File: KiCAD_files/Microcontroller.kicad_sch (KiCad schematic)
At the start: 87 parts, among them J403 RJ45_LED_Shielded, J404 RJ45_LED_Shielded, J405 Conn_01x02_Male, J406 Conn_01x02_Male, P401 Power2, U401 OwnTech_SPIN, U402 TCAN334GDR, U403 MCP1799T-5002H/TT, U404 AP1117-50, U405 LTC2850xS8, U406 OPA2277, U407 OPA316

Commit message: Closed open issues on TWIST V1.2. Cleaned the schematic and tweaked the routing files
Signed-off-by: Jean Alinei <jean.alinei@laas.fr>
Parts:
- removed C403, C406, C407: 10uF, Footprints:C_1210_3225Metric, symbol Device:C_Small
- removed C404, C405, C408, C409: 1uF, Footprints:C_0805_2012Metric, symbol Device:C_Small
- removed D401, D402: RBR2MM60ATFTR, Diode_SMD:D_SOD-123, symbol Device:D_Schottky_Small
- removed JP402: SolderJumper_2_Open, Jumper:SolderJumper-2_P1.3mm_Open_Pad1.0x1.5mm, symbol Jumper:SolderJumper_2_Open
- removed PS401: TEA 1-0505, Footprints:Converter_DCDC_Murata_MEE1SxxxxSC_THT, symbol Converter_DCDC:MEE1S0505SC
- removed PS402: TBA 1-0512, Footprints:Converter_DCDC_Murata_MEE1SxxxxSC_THT, symbol Converter_DCDC:MEE1S0512SC
- removed R421: 4.7k, Footprints:R_0805_2012Metric, symbol Device:R
- removed R424: 1k, Footprints:R_0805_2012Metric, symbol Device:R_Small
- removed U403: MCP1799T-5002H/TT, Footprints:SOT-23_copy, symbol Regulator_Linear:MCP1754S-5002xCB
- removed U404: AP1117-50, Package_TO_SOT_SMD:SOT-223-3_TabPin2, symbol Regulator_Linear:AP1117-50
- added unit 4 of U401
- C402: value 10uF -> 15nF; footprint Footprints:C_1210_3225Metric -> Footprints:C_0805_2012Metric; #manf 12105C106KAT2A -> (none); Manf# 12105C106KAT2A -> CC0805JRNPO9BN200
- F401, F402: footprint Fuse:Fuse_0805_2012Metric -> Fuse:Fuse_1210_3225Metric
- R408: value 1R -> 120R; Manf# CR0805-J/-1R0ELF -> CR0805-FX-4701ELF
- U406: value OPA2277 -> MCP6487T-E/SN
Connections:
- net GND_COM is gone; now on net DGND: J403.8, J404.8, J405.2 (Pin_2), J406.2 (Pin_2), R403.1, R405.1
- net +3V3: now also U401.36 (+3.3V); no longer U401.42 (+3.3V)
- net +5VD: now also C413.1, C415.1, U401.40 (+VIN), U406.8 (V+), U407.5 (V+); no longer C402.1, U401.46 (+VIN)
- net +6V: now also F401.1, F402.2
- net +BATT: now also U401.39 (+VBAT); no longer U401.45 (+VBAT)
- net ADC2_IN5: now also U401.35 (PC4); no longer U401.41 (PC4)
- net ADC3_IN12: now also U401.31 (PB0); no longer U401.37 (PB0)
- net DAC2: now also U401.34 (PA6); no longer U401.40 (PA6)
- net DGND: now also C402.1, U401.23 (GND), U401.28 (GND), U401.33 (GND), U401.38 (GND), U401.54 (GND), U401.57 (GND); no longer C402.2, R408.2, U401.22 (GND), U401.25 (GND), U401.29 (GND), U401.34 (GND), U401.39 (GND), U401.44 (GND)
- net FDCAN1_{RX}: now also U401.58 (PB8); no longer U401.26 (PB8)
- net FDCAN1_{TX}: now also U401.21 (PB9); no longer U401.27 (PB9)
- net HRTIM_CHA1: now also U401.12 (PA8); no longer U401.14 (PA9)
- net HRTIM_CHA2: now also U401.14 (PA9); no longer U401.12 (PA8)
- net I_{I1Low}: now also U401.30 (PA1); no longer U401.36 (PA1)
- net I_{I2Low}: now also U401.25 (PC1); no longer U401.31 (PC1)
- net I_{IHigh}: now also U401.26 (PC2); no longer U401.32 (PC2)
- net PB1: now also U401.37 (PB1); no longer U401.43 (PB1)
- net PB6: now also U401.55 (PB6); no longer U401.23 (PB6)
- net PC13: now also U401.22 (PC13); no longer U401.28 (PC13)
- net SHARE+: no longer R420.2
- net V_{I1Low}: now also U401.29 (PA0); no longer U401.35 (PA0)
- net V_{I2Low}: now also U401.24 (PC0); no longer U401.30 (PC0)
- net V_{IHigh}: now also U401.27 (PC3); no longer U401.33 (PC3)
- net at R408.1: now also C411.1, R415.1, U406.7
- net at R419.1, U406.5 (+): now also R420.2
- net CAN1_STB: no longer names the net of U402.8 (STB)
- new net: C402.2, JP410.2 (B), JP411.2 (B), R408.2
- no-connect marks 21 -> 23
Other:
- note added: "1.024V reference for measurement offset"
- note added: "CAN bus power supply - 6V - 100mA Polyfuse to prevent over-current in daisy-chained bus with multiple sources and sinks."
- note added: "Emitting circuit"
- note added: "Low pass filter Cut-off frequency 88.5kHz"
- note added: "Receiving circuit"
- note removed: "Alternate 1.024V VREF signal from SoC integrated DAC2. Conflicts with Analog share bus"
- note removed: "CAN bus power supply - 6V - 100mA Diodes necessary to prevent separate GND loops. Polyfuse to prevent over-current in daisy-chained bus with multiple sources and sinks."
- note removed: "DAC2 can be used to provide a reference if this fails"
- note removed: "Rudimentary 1.024V reference for measurement offset"
- moved on the sheet: C401, C410, C411, C412, C413, C414, C415, C416, D403, F401, F402, J403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

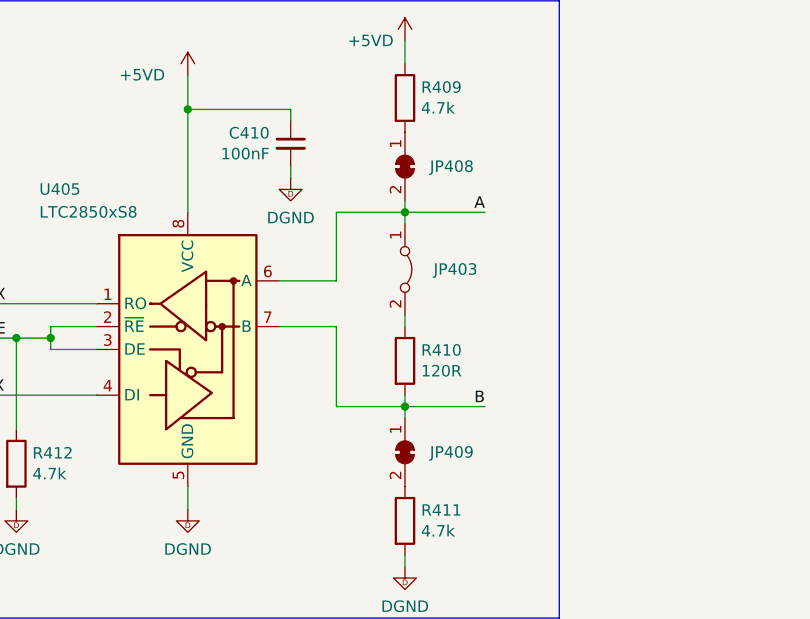
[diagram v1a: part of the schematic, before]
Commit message: Double check of each issue. Issue are now closed for V1.3
Signed-off-by: Jean Alinei <jean.alinei@laas.fr>
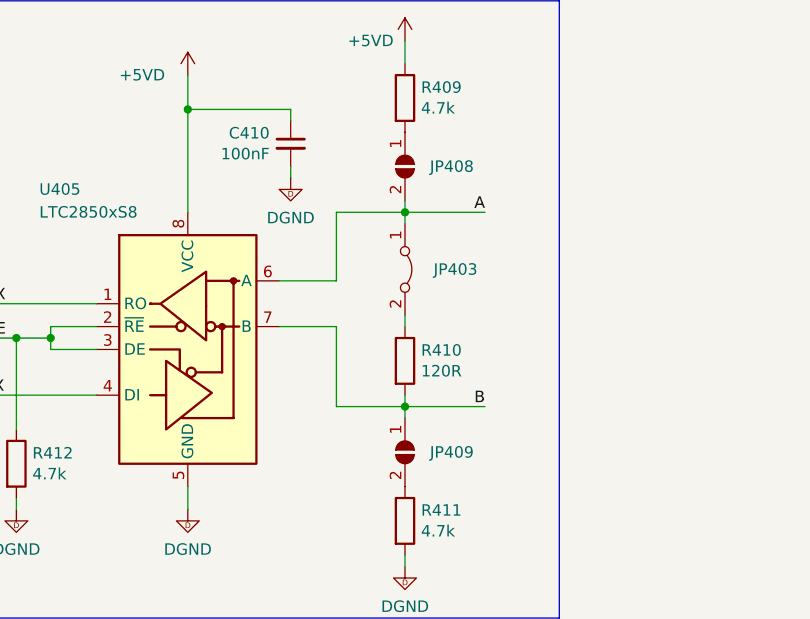
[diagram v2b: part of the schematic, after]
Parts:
- JP408, JP409: footprint Jumper:SolderJumper-2_P1.3mm_Bridged_Pad1.0x1.5mm -> Jumper:SolderJumper-2_P1.3mm_Open_RoundedPad1.0x1.5mm; symbol Jumper:SolderJumper_2_Bridged -> Jumper:SolderJumper_2_Open
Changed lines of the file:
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@@
     )
   )
-  (symbol (lib_id "Jumper:SolderJumper_2_Bridged") (at 264.16 171.45 270) (unit 1)
+  (symbol (lib_id "Jumper:SolderJumper_2_Open") (at 264.16 171.45 270) (unit 1)
     (in_bom yes) (on_board yes) (dnp no)
     (property "Reference" "JP409" (at 269.367 171.45 90)
@@
       (effects (font (size 1.27 1.27)) hide)
     )
-    (property "Footprint" "Jumper:SolderJumper-2_P1.3mm_Bridged_Pad1.0x1.5mm" (at 264.16 171.45 0)
+    (property "Footprint" "Jumper:SolderJumper-2_P1.3mm_Open_RoundedPad1.0x1.5mm" (at 264.16 171.45 0)
       (effects (font (size 1.27 1.27)) hide)
     )
@@
     )
   )
-  (symbol (lib_id "Jumper:SolderJumper_2_Bridged") (at 264.16 139.7 270) (unit 1)
+  (symbol (lib_id "Jumper:SolderJumper_2_Open") (at 264.16 139.7 270) (unit 1)
     (in_bom yes) (on_board yes) (dnp no)
     (property "Reference" "JP408" (at 269.367 139.7 90)
@@
       (effects (font (size 1.27 1.27)) hide)
     )
-    (property "Footprint" "Jumper:SolderJumper-2_P1.3mm_Bridged_Pad1.0x1.5mm" (at 264.16 139.7 0)
-      (effects (font (size 1.27 1.27)) hide)
-    )
+    (property "Footprint" "Jumper:SolderJumper-2_P1.3mm_Open_RoundedPad1.0x1.5mm" (at 264.16 139.7 0)
+      (effects (font (size 1.27 1.27)) hide)
+    )

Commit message: No more real ERC error
Signed-off-by: Jean Alinei <jean.alinei@laas.fr>
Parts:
- D403: footprint Footprints:D_SOD-323 -> Diode_SMD:D_SOD-323_HandSoldering
- JP404, JP406, JP411, JP412, JP413, JP414, JP415, JP417: footprint Jumper:SolderJumper-2_P1.3mm_Bridged_Pad1.0x1.5mm -> Jumper:SolderJumper-2_P1.3mm_Bridged_RoundedPad1.0x1.5mm
- JP407: value SolderJumper_2_Open -> SolderJumper; footprint Jumper:SolderJumper-2_P1.3mm_Bridged_Pad1.0x1.5mm -> Jumper:SolderJumper-2_P1.3mm_Bridged_RoundedPad1.0x1.5mm
- JP410: footprint Jumper:SolderJumper-2_P1.3mm_Open_Pad1.0x1.5mm -> Jumper:SolderJumper-2_P1.3mm_Open_RoundedPad1.0x1.5mm
- U401: footprint Footprints:SPIN_castellated_holes_board -> Footprints:OwnTech_SPINTHT
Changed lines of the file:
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@@
       (effects (font (size 1.27 1.27)) hide)
     )
-    (property "Footprint" "Jumper:SolderJumper-2_P1.3mm_Bridged_Pad1.0x1.5mm" (at 138.43 39.37 0)
+    (property "Footprint" "Jumper:SolderJumper-2_P1.3mm_Bridged_RoundedPad1.0x1.5mm" (at 138.43 39.37 0)
       (effects (font (size 1.27 1.27)) hide)
     )
@@
       (effects (font (size 1.27 1.27)))
     )
-    (property "Value" "SolderJumper_2_Open" (at 270.51 250.19 90)
+    (property "Value" "SolderJumper" (at 270.51 250.19 90)
       (effects (font (size 1.27 1.27)) hide)
     )
-    (property "Footprint" "Jumper:SolderJumper-2_P1.3mm_Bridged_Pad1.0x1.5mm" (at 267.97 236.22 0)
+    (property "Footprint" "Jumper:SolderJumper-2_P1.3mm_Bridged_RoundedPad1.0x1.5mm" (at 267.97 236.22 0)
       (effects (font (size 1.27 1.27)) hide)
     )
@@
       (effects (font (size 1.27 1.27)))
     )
-    (property "Footprint" "Footprints:D_SOD-323" (at 90.17 172.085 0)
+    (property "Footprint" "Diode_SMD:D_SOD-323_HandSoldering" (at 90.17 172.085 0)
       (effects (font (size 1.27 1.27)) hide)
     )
@@
       (effects (font (size 1.27 1.27)) hide)
     )
-    (property "Footprint" "Jumper:SolderJumper-2_P1.3mm_Bridged_Pad1.0x1.5mm" (at 135.89 57.15 0)
+    (property "Footprint" "Jumper:SolderJumper-2_P1.3mm_Bridged_RoundedPad1.0x1.5mm" (at 135.89 57.15 0)
       (effects (font (size 1.27 1.27)) hide)
     )
@@
       (effects (font (size 1.27 1.27)) hide)
     )
-    (property "Footprint" "Jumper:SolderJumper-2_P1.3mm_Bridged_Pad1.0x1.5mm" (at 135.89 50.8 0)
+    (property "Footprint" "Jumper:SolderJumper-2_P1.3mm_Bridged_RoundedPad1.0x1.5mm" (at 135.89 50.8 0)
       (effects (font (size 1.27 1.27)) hide)
     )
@@
       (effects (font (size 1.27 1.27)) hide)
     )
-    (property "Footprint" "Jumper:SolderJumper-2_P1.3mm_Open_Pad1.0x1.5mm" (at 124.46 146.05 0)
+    (property "Footprint" "Jumper:SolderJumper-2_P1.3mm_Open_RoundedPad1.0x1.5mm" (at 124.46 146.05 0)
       (effects (font (size 1.27 1.27)) hide)
     )
@@
       (effects (font (size 1.27 1.27)) hide)
     )
-    (property "Footprint" "Jumper:SolderJumper-2_P1.3mm_Bridged_Pad1.0x1.5mm" (at 133.35 27.94 0)
+    (property "Footprint" "Jumper:SolderJumper-2_P1.3mm_Bridged_RoundedPad1.0x1.5mm" (at 133.35 27.94 0)
       (effects (font (size 1.27 1.27)) hide)
     )
@@
       (effects (font (size 1.27 1.27)) hide)
     )
-    (property "Footprint" "Jumper:SolderJumper-2_P1.3mm_Bridged_Pad1.0x1.5mm" (at 41.91 165.1 0)
+    (property "Footprint" "Jumper:SolderJumper-2_P1.3mm_Bridged_RoundedPad1.0x1.5mm" (at 41.91 165.1 0)
       (effects (font (size 1.27 1.27)) hide)
     )
@@
       (effects (font (size 1.27 1.27)) hide)
     )
-    (property "Footprint" "Jumper:SolderJumper-2_P1.3mm_Bridged_Pad1.0x1.5mm" (at 133.35 33.02 0)
+    (property "Footprint" "Jumper:SolderJumper-2_P1.3mm_Bridged_RoundedPad1.0x1.5mm" (at 133.35 33.02 0)
       (effects (font (size 1.27 1.27)) hide)
     )
@@
       (effects (font (size 1.27 1.27)) hide)
     )
-    (property "Footprint" "Jumper:SolderJumper-2_P1.3mm_Bridged_Pad1.0x1.5mm" (at 133.35 21.59 0)
+    (property "Footprint" "Jumper:SolderJumper-2_P1.3mm_Bridged_RoundedPad1.0x1.5mm" (at 133.35 21.59 0)
       (effects (font (size 1.27 1.27)) hide)
     )
@@
       (effects (font (size 1.27 1.27)) hide)
     )
-    (property "Footprint" "Footprints:SPIN_castellated_holes_board" (at 154.305 90.805 0)
+    (property "Footprint" "Footprints:OwnTech_SPINTHT" (at 154.305 90.805 0)
       (effects (font (size 1.27 1.27)) hide)
     )
@@
       (effects (font (size 1.27 1.27)) hide)
     )
-    (property "Footprint" "Jumper:SolderJumper-2_P1.3mm_Bridged_Pad1.0x1.5mm" (at 124.46 152.4 0)
+    (property "Footprint" "Jumper:SolderJumper-2_P1.3mm_Bridged_RoundedPad1.0x1.5mm" (at 124.46 152.4 0)
       (effects (font (size 1.27 1.27)) hide)
     )
@@
       (effects (font (size 1.27 1.27)) hide)
     )
-    (property "Footprint" "Jumper:SolderJumper-2_P1.3mm_Bridged_Pad1.0x1.5mm" (at 138.43 44.45 0)
+    (property "Footprint" "Jumper:SolderJumper-2_P1.3mm_Bridged_RoundedPad1.0x1.5mm" (at 138.43 44.45 0)
       (effects (font (size 1.27 1.27)) hide)
     )

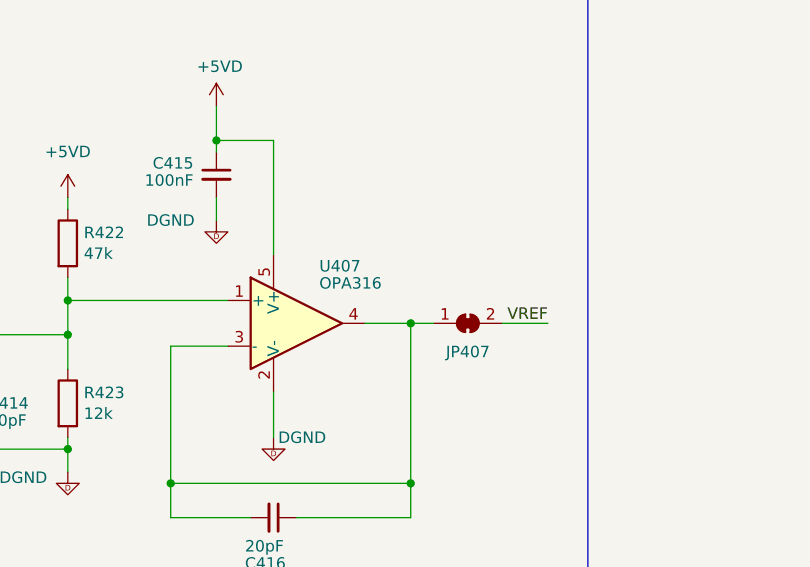
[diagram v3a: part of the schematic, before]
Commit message: Fixed mechanical issues with front plate and corrected guard ring footprint. General position of the routing is now correctly aligned with 1mm grid.
Signed-off-by: Jean Alinei <jean.alinei@laas.fr>
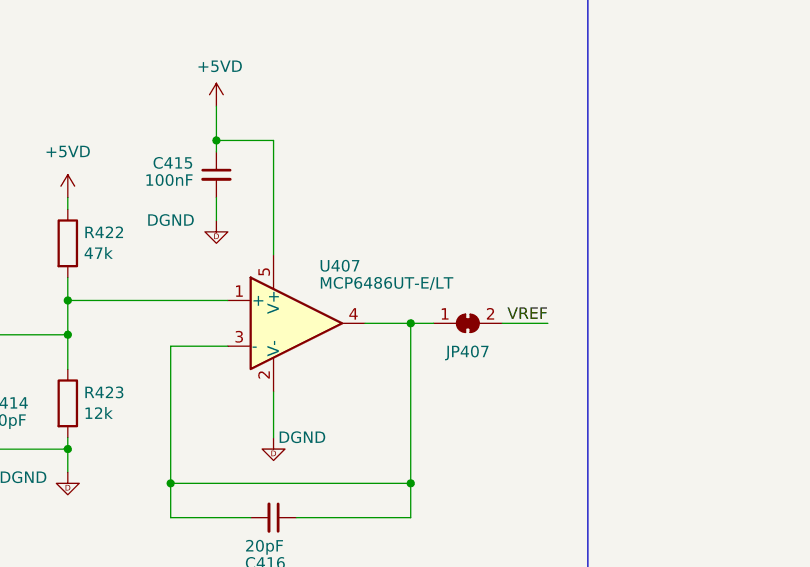
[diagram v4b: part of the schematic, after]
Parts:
- U407: value OPA316 -> MCP6486UT-E/LT; footprint Package_TO_SOT_SMD:SOT-353_SC-70-5 -> Package_TO_SOT_SMD:SOT-353_SC-70-5_Handsoldering
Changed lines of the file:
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@@
       (effects (font (size 1.27 1.27)) (justify left))
     )
-    (property "Value" "OPA316" (at 251.46 231.775 0)
+    (property "Value" "MCP6486UT-E/LT " (at 251.46 231.775 0)
       (effects (font (size 1.27 1.27)) (justify left))
     )
-    (property "Footprint" "Package_TO_SOT_SMD:SOT-353_SC-70-5" (at 251.46 236.22 0)
+    (property "Footprint" "Package_TO_SOT_SMD:SOT-353_SC-70-5_Handsoldering" (at 251.46 236.22 0)
       (effects (font (size 1.27 1.27)) hide)
     )

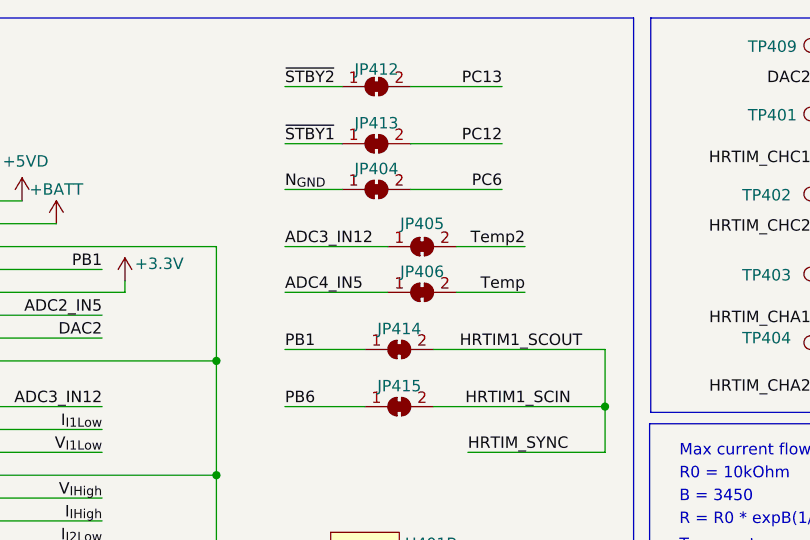
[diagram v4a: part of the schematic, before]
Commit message: Added a dual footprint that includes both WAGO terminals and eurorack DIN41612 terminal
Signed-off-by: Jean Alinei <jean.alinei@laas.fr>
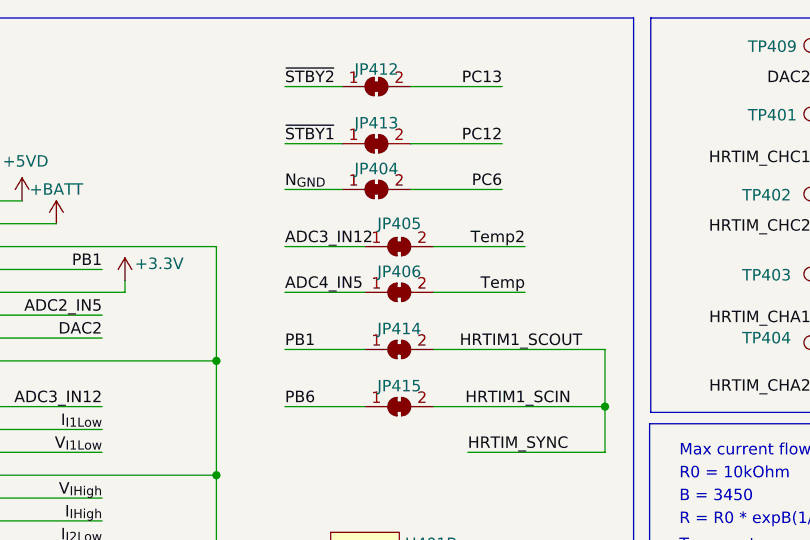
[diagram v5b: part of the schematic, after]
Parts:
- TH401, TH402: footprint Connector_PinHeader_1.27mm:PinHeader_1x02_P1.27mm_Horizontal -> Connector_PinHeader_1.27mm:PinHeader_1x02_P1.27mm_Vertical
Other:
- moved on the sheet: JP405, JP406
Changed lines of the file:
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@@
     (stroke (width 0) (type default))
   )
-  (wire (pts (xy 123.19 39.37) (xy 134.62 39.37))
+  (wire (pts (xy 123.19 39.37) (xy 132.08 39.37))
     (stroke (width 0) (type default))
   )
@@
     (stroke (width 0) (type default))
   )
-  (wire (pts (xy 123.19 44.45) (xy 134.62 44.45))
+  (wire (pts (xy 123.19 44.45) (xy 132.08 44.45))
     (stroke (width 0) (type default))
   )
@@
     (stroke (width 0) (type default))
   )
-  (wire (pts (xy 142.24 39.37) (xy 149.86 39.37))
+  (wire (pts (xy 139.7 39.37) (xy 149.86 39.37))
     (stroke (width 0) (type default))
   )
@@
     (stroke (width 0) (type default))
   )
-  (wire (pts (xy 142.24 44.45) (xy 149.86 44.45))
+  (wire (pts (xy 139.7 44.45) (xy 149.86 44.45))
     (stroke (width 0) (type default))
   )
@@
       (effects (font (size 1.27 1.27)) (justify left))
     )
-    (property "Footprint" "Connector_PinHeader_1.27mm:PinHeader_1x02_P1.27mm_Horizontal" (at 168.91 104.14 0)
+    (property "Footprint" "Connector_PinHeader_1.27mm:PinHeader_1x02_P1.27mm_Vertical" (at 168.91 104.14 0)
       (effects (font (size 1.27 1.27)) hide)
     )
@@
     )
   )
-  (symbol (lib_id "Jumper:SolderJumper_2_Bridged") (at 138.43 39.37 0) (unit 1)
+  (symbol (lib_id "Jumper:SolderJumper_2_Bridged") (at 135.89 39.37 0) (unit 1)
     (in_bom yes) (on_board yes) (dnp no)
-    (property "Reference" "JP405" (at 138.43 36.83 0)
+    (property "Reference" "JP405" (at 135.89 36.83 0)
       (effects (font (size 1.27 1.27)))
     )
-    (property "Value" "Jumper_2_Bridged" (at 138.43 36.195 0)
+    (property "Value" "Jumper_2_Bridged" (at 135.89 36.195 0)
       (effects (font (size 1.27 1.27)) hide)
     )
-    (property "Footprint" "Jumper:SolderJumper-2_P1.3mm_Bridged_RoundedPad1.0x1.5mm" (at 138.43 39.37 0)
+    (property "Footprint" "Jumper:SolderJumper-2_P1.3mm_Bridged_RoundedPad1.0x1.5mm" (at 135.89 39.37 0)
       (effects (font (size 1.27 1.27)) hide)
     )
-    (property "Datasheet" "" (at 138.43 39.37 0)
+    (property "Datasheet" "" (at 135.89 39.37 0)
       (effects (font (size 1.27 1.27)) hide)
     )
-    (property "Datasheet" "" (at 138.43 39.37 0)
+    (property "Datasheet" "" (at 135.89 39.37 0)
       (effects (font (size 1.27 1.27)) hide)
     )
-    (property "Footprint" "Jumper:SolderJumper-2_P1.3mm_Bridged_Pad1.0x1.5mm" (at 138.43 39.37 0)
+    (property "Footprint" "Jumper:SolderJumper-2_P1.3mm_Bridged_Pad1.0x1.5mm" (at 135.89 39.37 0)
       (effects (font (size 1.27 1.27)) hide)
     )
-    (property "Reference" "JP405" (at 138.43 39.37 0)
+    (property "Reference" "JP405" (at 135.89 39.37 0)
       (effects (font (size 1.27 1.27)) hide)
     )
-    (property "Value" "Jumper_2_Bridged" (at 138.43 39.37 0)
+    (property "Value" "Jumper_2_Bridged" (at 135.89 39.37 0)
       (effects (font (size 1.27 1.27)) hide)
     )
-    (property "DNP" "x" (at 138.43 39.37 0)
+    (property "DNP" "x" (at 135.89 39.37 0)
       (effects (font (size 1.27 1.27)) hide)
     )
@@
       (effects (font (size 1.27 1.27)) (justify left))
     )
-    (property "Footprint" "Connector_PinHeader_1.27mm:PinHeader_1x02_P1.27mm_Horizontal" (at 194.31 104.14 0)
+    (property "Footprint" "Connector_PinHeader_1.27mm:PinHeader_1x02_P1.27mm_Vertical" (at 194.31 104.14 0)
       (effects (font (size 1.27 1.27)) hide)
     )
@@
     )
   )
-  (symbol (lib_id "Jumper:SolderJumper_2_Bridged") (at 138.43 44.45 0) (unit 1)
+  (symbol (lib_id "Jumper:SolderJumper_2_Bridged") (at 135.89 44.45 0) (unit 1)
     (in_bom yes) (on_board yes) (dnp no)
-    (property "Reference" "JP406" (at 138.43 42.164 0)
+    (property "Reference" "JP406" (at 135.89 42.164 0)
       (effects (font (size 1.27 1.27)))
     )
-    (property "Value" "Jumper_2_Bridged" (at 138.43 41.275 0)
+    (property "Value" "Jumper_2_Bridged" (at 135.89 41.275 0)
       (effects (font (size 1.27 1.27)) hide)
     )
-    (property "Footprint" "Jumper:SolderJumper-2_P1.3mm_Bridged_RoundedPad1.0x1.5mm" (at 138.43 44.45 0)
+    (property "Footprint" "Jumper:SolderJumper-2_P1.3mm_Bridged_RoundedPad1.0x1.5mm" (at 135.89 44.45 0)
       (effects (font (size 1.27 1.27)) hide)
     )
-    (property "Datasheet" "~" (at 138.43 44.45 0)
+    (property "Datasheet" "~" (at 135.89 44.45 0)
       (effects (font (size 1.27 1.27)) hide)
     )
-    (property "DNP" "x" (at 138.43 44.45 0)
+    (property "DNP" "x" (at 135.89 44.45 0)
       (effects (font (size 1.27 1.27)) hide)
     )
